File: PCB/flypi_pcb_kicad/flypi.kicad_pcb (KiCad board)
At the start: 2 copper layers, 76 x 93 mm, 44 parts, among them CON1 BARREL_JACK, J12 USB_A, P1 PeltS1S2, P10 RGB RG-B, P3 Fan+-, P4 Therm +s-, P5 HP1+-, P6 HP2+-, P7 servo +s-, P8 Ring +-s, P9 matrix +-scsd, Q1 1A_NPN_ECB, Q2 1A-NPN-ECB, Q3 1A_NPN_ECB, Q4 1A_NPN_ECB, U1 LM2596, U2 LM2596, U3 LM2596, U4 L298N, U5 arduino_mini

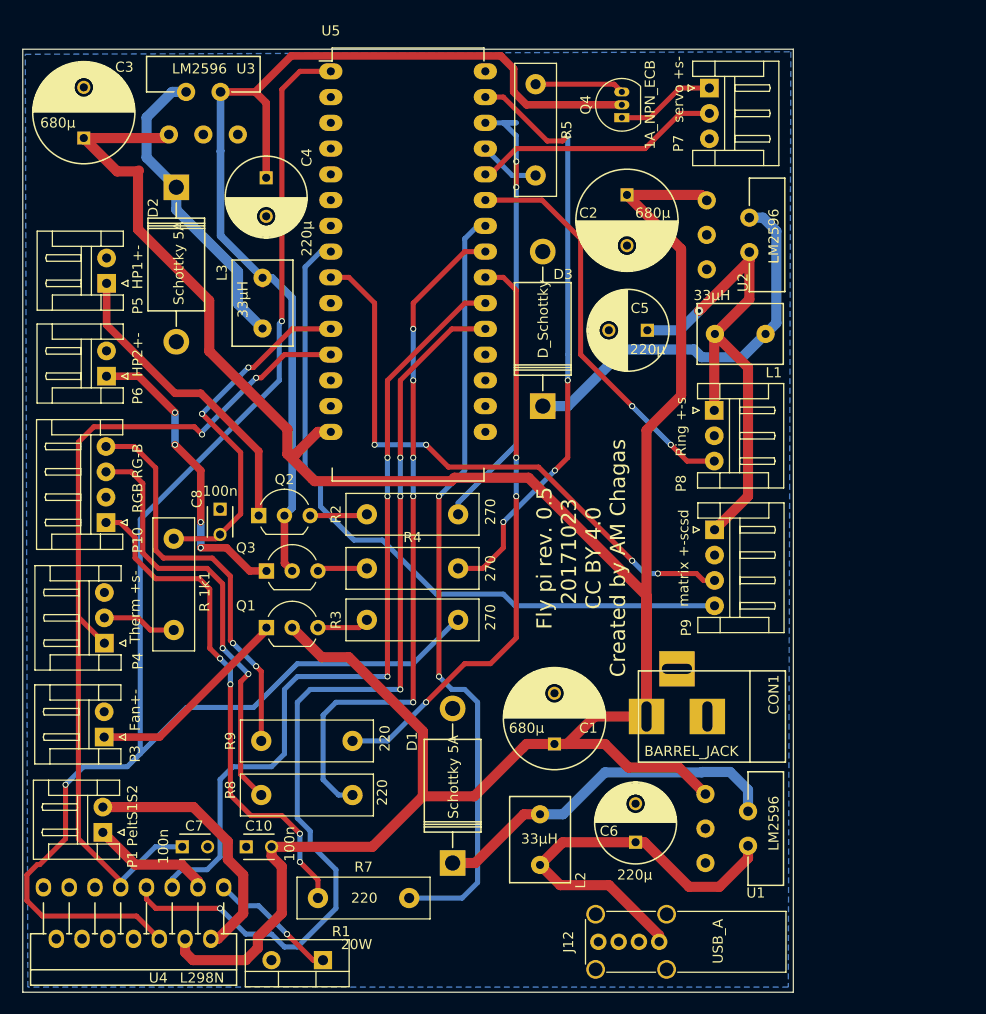
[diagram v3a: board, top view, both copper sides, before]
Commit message: update to pcb labels (corrected inverted values)
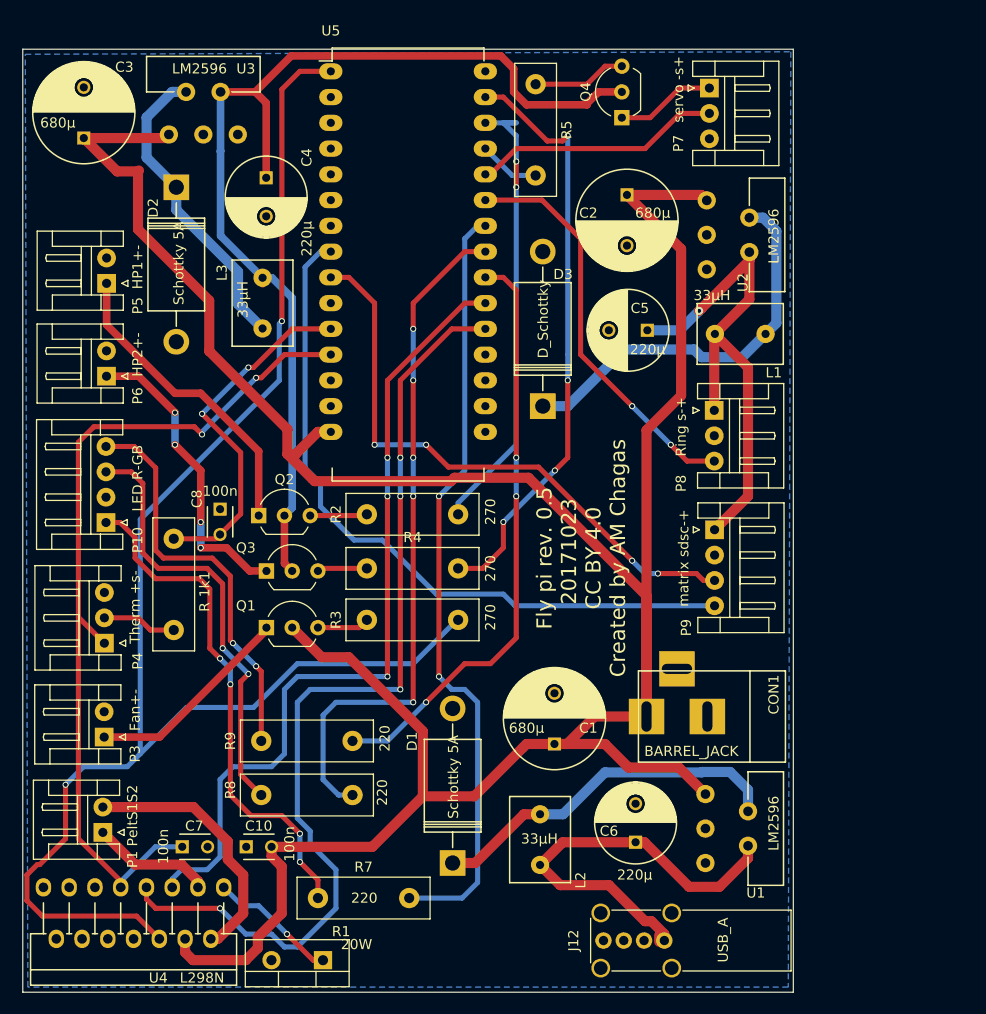
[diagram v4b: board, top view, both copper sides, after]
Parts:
- P10: value RGB RG-B -> LED R-GB
- P7: value servo +s- -> servo -s+
- P8: value Ring +-s -> Ring s-+
- P9: value matrix +-scsd -> matrix sdsc-+
- Q4: footprint TO_SOT_Packages_THT:TO-92_Inline_Narrow_Oval -> TO_SOT_Packages_THT:TO-92_Inline_Wide
- moved J12 0.52 mm to (168.3, 128.9)
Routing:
- net Net-(C6-Pad1): track 40.9 -> 42.0 mm
- net Net-(C4-Pad1): track 105.3 -> 105.9 mm
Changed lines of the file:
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@@
     (thickness 1.6)
     (drawings 12)
-    (tracks 445)
+    (tracks 452)
     (zones 0)
     (modules 44)
@@
   )
   (module Connectors:USB_A_Vertical (layer F.Cu)
-    (at 167.77 129.03 270)
+    (at 168.275 128.905 270)
     (descr "USB A vertical female connector, right angle")
     (tags "USB_A_Vertical female connector angled 73725-0110BLF")
@@
       (effects (font (size 1 1) (thickness 0.15)))
     )
-    (fp_text value "servo +s-" (at 0.128 3.048 270) (layer F.SilkS)
+    (fp_text value "servo -s+" (at 0.128 3.048 270) (layer F.SilkS)
       (effects (font (size 1 1) (thickness 0.15)))
     )
@@
       (effects (font (size 1 1) (thickness 0.15)))
     )
-    (fp_text value "Ring +-s" (at 1.612 3.274 270) (layer F.SilkS)
+    (fp_text value "Ring s-+" (at 1.612 3.274 270) (layer F.SilkS)
       (effects (font (size 1 1) (thickness 0.15)))
     )
@@
       (effects (font (size 1 1) (thickness 0.15)))
     )
-    (fp_text value "matrix +-scsd" (at 2.796 3.05 270) (layer F.SilkS)
+    (fp_text value "matrix sdsc-+" (at 2.796 3.05 270) (layer F.SilkS)
       (effects (font (size 1 1) (thickness 0.15)))
     )
@@
       (effects (font (size 1 1) (thickness 0.15)))
     )
-    (fp_text value "RGB RG-B" (at 4.368 3.122 90) (layer F.SilkS)
+    (fp_text value "LED R-GB" (at 4.368 3.122 90) (layer F.SilkS)
       (effects (font (size 1 1) (thickness 0.15)))
     )
@@
     )
   )
-  (module TO_SOT_Packages_THT:TO-92_Inline_Narrow_Oval (layer F.Cu)
-    (at 164.084 47.752 90)
-    (descr "TO-92 leads in-line, narrow, oval pads, drill 0.6mm (see NXP sot054_po.pdf)")
-    (tags "to-92 sc-43 sc-43a sot54 PA33 transistor")
-    (fp_text reference Q4 (at 1.27 -3.56 90) (layer F.SilkS)
-      (effects (font (size 1 1) (thickness 0.15)))
-    )
-    (fp_text value 1A_NPN_ECB (at 1.27 2.79 90) (layer F.SilkS)
-      (effects (font (size 1 1) (thickness 0.15)))
-    )
-    (fp_text user %R (at 1.27 -3.56 90) (layer F.Fab)
-      (effects (font (size 1 1) (thickness 0.15)))
-    )
-    (fp_line (start -0.53 1.85) (end 3.07 1.85) (layer F.SilkS) (width 0.12))
-    (fp_line (start -0.5 1.75) (end 3 1.75) (layer F.Fab) (width 0.1))
-    (fp_line (start -1.46 -2.73) (end 4 -2.73) (layer F.CrtYd) (width 0.05))
-    (fp_line (start -1.46 -2.73) (end -1.46 2.01) (layer F.CrtYd) (width 0.05))
-    (fp_line (start 4 2.01) (end 4 -2.73) (layer F.CrtYd) (width 0.05))
-    (fp_line (start 4 2.01) (end -1.46 2.01) (layer F.CrtYd) (width 0.05))
-    (fp_arc (start 1.27 0) (end 1.27 -2.48) (angle 135) (layer F.Fab) (width 0.1))
-    (fp_arc (start 1.27 0) (end 1.27 -2.6) (angle -135) (layer F.SilkS) (width 0.12))
-    (fp_arc (start 1.27 0) (end 1.27 -2.48) (angle -135) (layer F.Fab) (width 0.1))
-    (fp_arc (start 1.27 0) (end 1.27 -2.6) (angle 135) (layer F.SilkS) (width 0.12))
-    (pad 2 thru_hole oval (at 1.27 0 270) (size 0.9 1.5) (drill 0.6) (layers *.Cu *.Mask)
-      (net 4 "Net-(C4-Pad1)"))
-    (pad 3 thru_hole oval (at 2.54 0 270) (size 0.9 1.5) (drill 0.6) (layers *.Cu *.Mask)
-      (net 27 "Net-(Q4-Pad3)"))
-    (pad 1 thru_hole rect (at 0 0 270) (size 0.9 1.5) (drill 0.6) (layers *.Cu *.Mask)
-      (net 17 "Net-(P7-Pad1)"))
-    (model ${KISYS3DMOD}/TO_SOT_Packages_THT.3dshapes/TO-92_Inline_Narrow_Oval.wrl
-      (at (xyz 0.05 0 0))
-      (scale (xyz 1 1 1))
-      (rotate (xyz 0 0 -90))
-    )
-  )
   (module TO_SOT_Packages_THT:TO-220-2_Vertical (layer F.Cu)
     (at 134.61 130.84 180)
@@
     (pad 1 thru_hole rect (at 0 0 90) (size 1.52 1.52) (drill 0.8) (layers *.Cu *.Mask)
       (net 13 "Net-(P3-Pad1)"))
+    (model ${KISYS3DMOD}/TO_SOT_Packages_THT.3dshapes/TO-92_Inline_Wide.wrl
+      (at (xyz 0.1 0 0))
+      (scale (xyz 1 1 1))
+      (rotate (xyz 0 0 -90))
+    )
+  )
+  (module TO_SOT_Packages_THT:TO-92_Inline_Wide (layer F.Cu)
+    (at 164.084 47.752 90)
+    (descr "TO-92 leads in-line, wide, drill 0.8mm (see NXP sot054_po.pdf)")
+    (tags "to-92 sc-43 sc-43a sot54 PA33 transistor")
+    (fp_text reference Q4 (at 2.54 -3.56 270) (layer F.SilkS)
+      (effects (font (size 1 1) (thickness 0.15)))
+    )
+    (fp_text value 1A_NPN_ECB (at 2.54 2.79 90) (layer F.Fab)
+      (effects (font (size 1 1) (thickness 0.15)))
+    )
+    (fp_text user %R (at 2.54 -3.56 270) (layer F.Fab)
+      (effects (font (size 1 1) (thickness 0.15)))
+    )
+    (fp_line (start 0.74 1.85) (end 4.34 1.85) (layer F.SilkS) (width 0.12))
+    (fp_line (start 0.8 1.75) (end 4.3 1.75) (layer F.Fab) (width 0.1))
+    (fp_line (start -1.01 -2.73) (end 6.09 -2.73) (layer F.CrtYd) (width 0.05))
+    (fp_line (start -1.01 -2.73) (end -1.01 2.01) (layer F.CrtYd) (width 0.05))
+    (fp_line (start 6.09 2.01) (end 6.09 -2.73) (layer F.CrtYd) (width 0.05))
+    (fp_line (start 6.09 2.01) (end -1.01 2.01) (layer F.CrtYd) (width 0.05))
+    (fp_arc (start 2.54 0) (end 0.74 1.85) (angle 20) (layer F.SilkS) (width 0.12))
+    (fp_arc (start 2.54 0) (end 2.54 -2.6) (angle -65) (layer F.SilkS) (width 0.12))
+    (fp_arc (start 2.54 0) (end 2.54 -2.6) (angle 65) (layer F.SilkS) (width 0.12))
+    (fp_arc (start 2.54 0) (end 2.54 -2.48) (angle 135) (layer F.Fab) (width 0.1))
+    (fp_arc (start 2.54 0) (end 2.54 -2.48) (angle -135) (layer F.Fab) (width 0.1))
+    (fp_arc (start 2.54 0) (end 4.34 1.85) (angle -20) (layer F.SilkS) (width 0.12))
+    (pad 2 thru_hole circle (at 2.54 0 180) (size 1.52 1.52) (drill 0.8) (layers *.Cu *.Mask)
+      (net 4 "Net-(C4-Pad1)"))
+    (pad 3 thru_hole circle (at 5.08 0 180) (size 1.52 1.52) (drill 0.8) (layers *.Cu *.Mask)
+      (net 27 "Net-(Q4-Pad3)"))
+    (pad 1 thru_hole rect (at 0 0 180) (size 1.52 1.52) (drill 0.8) (layers *.Cu *.Mask)
+      (net 17 "Net-(P7-Pad1)"))
     (model ${KISYS3DMOD}/TO_SOT_Packages_THT.3dshapes/TO-92_Inline_Wide.wrl
       (at (xyz 0.1 0 0))
@@
   (segment (start 158.15 109.52) (end 157.44 109.52) (width 1) (layer F.Cu) (net 3))
   (segment (start 161.4 106.81) (end 158.69 109.52) (width 1) (layer F.Cu) (net 3))
+  (segment (start 160.655 46.482) (end 160.655 46.355) (width 0.75) (layer F.Cu) (net 4))
+  (segment (start 161.798 45.212) (end 164.084 45.212) (width 0.75) (layer F.Cu) (net 4))
+  (segment (start 160.655 46.355) (end 161.798 45.212) (width 0.75) (layer F.Cu) (net 4))
   (segment (start 130.81 86.995) (end 130.81 91.694) (width 0.75) (layer F.Cu) (net 4))
   (segment (start 130.81 91.694) (end 131.572 92.456) (width 0.75) (layer F.Cu) (net 4))
@@
   (segment (start 131.572 65.532) (end 131.572 86.233) (width 0.75) (layer B.Cu) (net 4))
   (segment (start 129.58064 63.54064) (end 131.572 65.532) (width 0.75) (layer B.Cu) (net 4))
-  (segment (start 164.084 46.482) (end 154.686 46.482) (width 0.75) (layer F.Cu) (net 4))
+  (segment (start 160.655 46.482) (end 154.686 46.482) (width 0.75) (layer F.Cu) (net 4))
   (segment (start 131.484 41.656) (end 127.93 45.21) (width 0.75) (layer F.Cu) (net 4))
   (segment (start 152.146 41.656) (end 131.484 41.656) (width 0.75) (layer F.Cu) (net 4))
@@
   (segment (start 176.66 61.01) (end 176.66 65.68064) (width 1) (layer F.Cu) (net 5))
   (segment (start 176.66 65.68064) (end 173.26064 69.08) (width 1) (layer F.Cu) (net 5))
+  (segment (start 166.37 127) (end 167.005 127) (width 1) (layer F.Cu) (net 6))
+  (segment (start 167.005 127) (end 168.275 128.27) (width 1) (layer F.Cu) (net 6))
+  (segment (start 168.275 128.27) (end 168.275 128.905) (width 1) (layer F.Cu) (net 6))
   (segment (start 167.77 129.03) (end 167.77 128.4) (width 1) (layer F.Cu) (net 6))
-  (segment (start 167.77 128.4) (end 162.814 123.444) (width 1) (layer F.Cu) (net 6))
+  (segment (start 166.37 127) (end 162.814 123.444) (width 1) (layer F.Cu) (net 6))
   (segment (start 162.814 123.444) (end 158.01464 123.444) (width 1) (layer F.Cu) (net 6))
   (segment (start 158.01464 123.444) (end 156.02 121.44936) (width 1) (layer F.Cu) (net 6))
@@
   (segment (start 134.366 92.202) (end 134.112 92.456) (width 0.5) (layer F.Cu) (net 26))
   (segment (start 138.684 91.948) (end 138.938 92.202) (width 0.5) (layer F.Cu) (net 26))
-  (segment (start 155.58 44.45) (end 163.322 44.45) (width 0.5) (layer F.Cu) (net 27))
-  (segment (start 163.322 44.45) (end 164.084 45.212) (width 0.5) (layer F.Cu) (net 27))
+  (segment (start 155.58 44.45) (end 160.655 44.45) (width 0.5) (layer F.Cu) (net 27))
+  (segment (start 162.433 42.672) (end 164.084 42.672) (width 0.5) (layer F.Cu) (net 27))
+  (segment (start 160.655 44.45) (end 162.433 42.672) (width 0.5) (layer F.Cu) (net 27))
   (segment (start 150.622 48.26) (end 153.67 48.26) (width 0.5) (layer B.Cu) (net 28))
   (segment (start 147.938 85.742) (end 147.938 86.868) (width 0.5) (layer B.Cu) (net 28))

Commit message: updated the PCB. Removed one of the voltage regulators (as everything seem to work fine with just 2. Changed the plugs so that the cables cab be bought crimmped.)
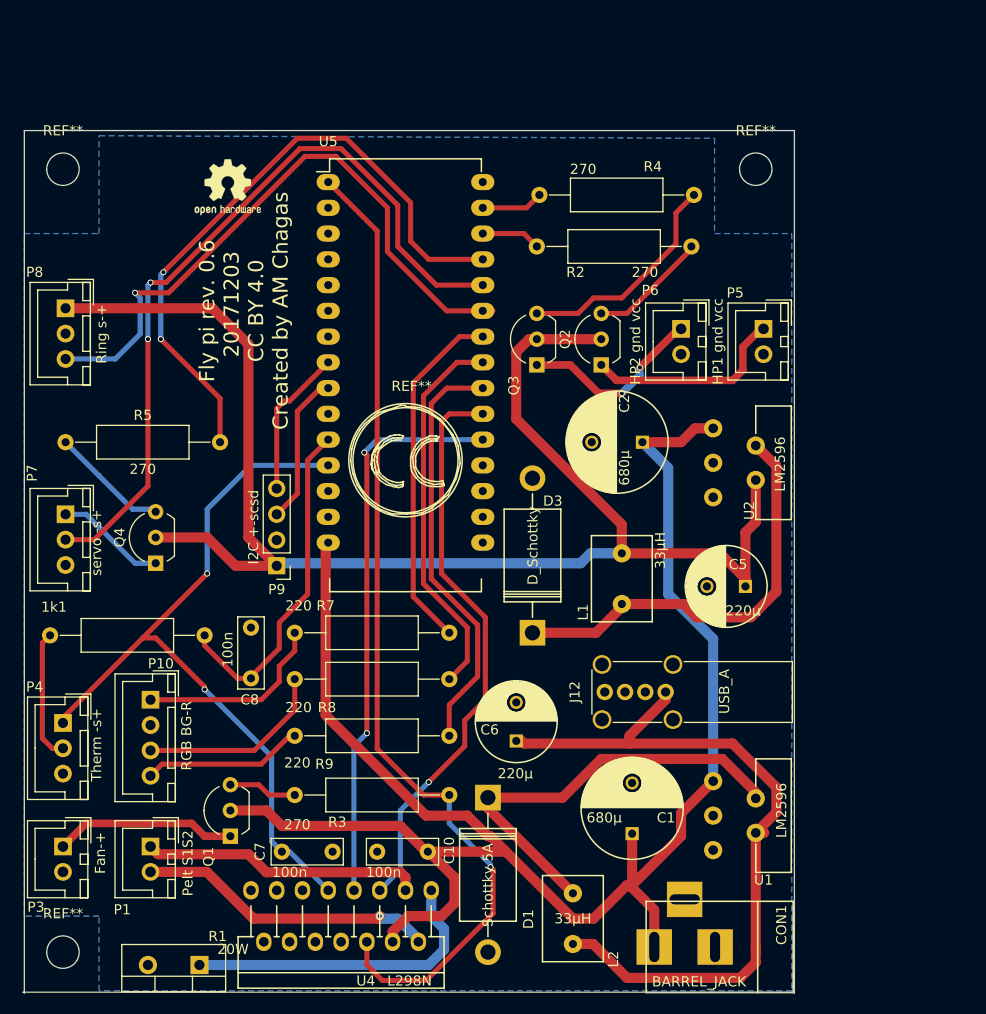
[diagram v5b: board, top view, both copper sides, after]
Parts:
- removed C3: 680µ, Capacitors_ThroughHole:C_Radial_D10_L21_P5
- removed C4: 220µ, Capacitors_ThroughHole:C_Radial_D8_L13_P3.8
- removed D2: Schottky 5A, Diodes_ThroughHole:Diode_DO-201AD_Horizontal_RM15
- removed L3: 33µH, Inductors_NEOSID:Neosid_Inductor_MA-Bs75
- removed U3: LM2596, footprints:LM2596
- added REF**: MountingHole_3.2mm_M3_DIN965, Mounting_Holes:MountingHole_3.2mm_M3_DIN965, F.Cu at (109.0, 130.0)
- added REF**: MountingHole_3.2mm_M3_DIN965, Mounting_Holes:MountingHole_3.2mm_M3_DIN965, F.Cu at (109.0, 52.8)
- added REF**: MountingHole_3.2mm_M3_DIN965, Mounting_Holes:MountingHole_3.2mm_M3_DIN965, F.Cu at (177.3, 52.8)
- added REF**: Symbol_CreativeCommons_SilkScreenTop_Type2_Big, Symbols:Symbol_CreativeCommons_SilkScreenTop_Type2_Big, F.Cu at (142.7, 81.5)
- added REF***: OSHW-Logo2_7.3x6mm_SilkScreen, Symbols:OSHW-Logo2_7.3x6mm_SilkScreen, F.Cu at (125.2, 54.6)
- 1k1, R2, R3, R4, R5, R7, R8, R9: footprint Resistors_THT:R_Box_L13.0mm_W4.0mm_P9.00mm -> Resistors_THT:R_Axial_DIN0309_L9.0mm_D3.2mm_P15.24mm_Horizontal
- C10, C7, C8: footprint Capacitors_ThroughHole:C_Disc_D3_P2.5 -> Capacitors_THT:C_Rect_L7.0mm_W2.5mm_P5.00mm
- P1: value PeltS1S2 -> Pelt S1S2; footprint Connectors_JST:JST_EH_S02B-EH_02x2.50mm_Angled -> Connectors_JST:JST_XH_B02B-XH-A_02x2.50mm_Straight
- P10: value LED R-GB -> RGB BG-R; footprint Connectors_JST:JST_EH_S04B-EH_04x2.50mm_Angled -> Connectors_JST:JST_XH_B04B-XH-A_04x2.50mm_Straight
- P3: value Fan+- -> Fan-+; footprint Connectors_JST:JST_EH_S02B-EH_02x2.50mm_Angled -> Connectors_JST:JST_XH_B02B-XH-A_02x2.50mm_Straight
- P4: value Therm +s- -> Therm -s+; footprint Connectors_JST:JST_EH_S03B-EH_03x2.50mm_Angled -> Connectors_JST:JST_XH_B03B-XH-A_03x2.50mm_Straight
- P5: value HP1+- -> HP1 gnd vcc; footprint Connectors_JST:JST_EH_S02B-EH_02x2.50mm_Angled -> Connectors_JST:JST_XH_B02B-XH-A_02x2.50mm_Straight
- P6: value HP2+- -> HP2 gnd vcc; footprint Connectors_JST:JST_EH_S02B-EH_02x2.50mm_Angled -> Connectors_JST:JST_XH_B02B-XH-A_02x2.50mm_Straight
- P7, P8: footprint Connectors_JST:JST_EH_S03B-EH_03x2.50mm_Angled -> Connectors_JST:JST_XH_B03B-XH-A_03x2.50mm_Straight
- P9: value matrix sdsc-+ -> I2C +-scsd; footprint Connectors_JST:JST_EH_S04B-EH_04x2.50mm_Angled -> Socket_Strips:Socket_Strip_Straight_1x04_Pitch2.54mm
- moved P7 76.2 mm to (109.2, 86.9)
- moved P5 64.9 mm to (178.1, 68.6), turned to 270 degrees
- moved P8 64.8 mm to (109.2, 66.5)
- moved Q4 63.6 mm to (118.1, 91.7)
- moved R5 58.3 mm to (109.2, 79.8), turned to 0 degrees
- moved P6 56.9 mm to (169.9, 68.6), turned to 270 degrees
- moved R4 49.0 mm to (171.2, 55.4), turned to 180 degrees
- moved P9 43.3 mm to (130.0, 91.9), turned to 180 degrees
- moved R2 41.5 mm to (170.9, 60.5), turned to 180 degrees
- moved Q2 36.9 mm to (162.1, 72.1), turned to 90 degrees
- moved Q3 33.5 mm to (155.7, 72.1), turned to 90 degrees
- moved C5 27.0 mm to (176.3, 94.0)
- moved L1 26.8 mm to (164.1, 93.2), turned to 90 degrees
- moved R7 26.3 mm to (131.8, 98.6)
- moved J12 24.5 mm to (168.4, 104.4)
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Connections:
- J12 pad 2: Net-(J12-Pad2) -> (no net)
- J12 pad 3: Net-(J12-Pad3) -> (no net)
- Q2 pad 2: Net-(C4-Pad1) -> Net-(C5-Pad1)
- Q3 pad 2: Net-(C4-Pad1) -> Net-(C5-Pad1)
- Q4 pad 2: Net-(C4-Pad1) -> Net-(C5-Pad1)
- U4 pad 10: Net-(U4-Pad10) -> (no net)
- U4 pad 11: Net-(U4-Pad11) -> (no net)
- U4 pad 12: Net-(U4-Pad12) -> (no net)
- U4 pad 13: Net-(U4-Pad13) -> (no net)
- U4 pad 14: Net-(U4-Pad14) -> (no net)
- U4 pad 15: Net-(U4-Pad15) -> (no net)
- U5 pad 10: Net-(U5-Pad10) -> (no net)
- U5 pad 13: Net-(U5-Pad13) -> (no net)
- U5 pad 16: Net-(U5-Pad16) -> (no net)
- U5 pad 17: Net-(U5-Pad17) -> (no net)
- U5 pad 18: Net-(U5-Pad18) -> (no net)
- U5 pad 2: Net-(U5-Pad2) -> (no net)
- U5 pad 3: Net-(U5-Pad3) -> (no net)
- U5 pad 30: Net-(U5-Pad30) -> (no net)
- U5 pad 4: Net-(U5-Pad4) -> (no net)
- U5 pad 5: Net-(U5-Pad5) -> (no net)
- U5 pad 6: Net-(U5-Pad6) -> (no net)
- U5 pad 7: Net-(U5-Pad7) -> (no net)
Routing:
- net Net-(C4-Pad1): track 105.9 -> 0.00 mm
- net Net-(C1-Pad1): track 273.8 -> 170.1 mm
- net Net-(C5-Pad1): track 52.8 -> 148.1 mm, vias 1 -> 0
- net Net-(R5-Pad2): track 6.07 -> 63.4 mm, vias 0 -> 2
- net Net-(P9-Pad4): track 70.3 -> 14.8 mm
- net Net-(R4-Pad2): track 58.7 -> 6.11 mm, vias 4 -> 0
- net Net-(R3-Pad2): track 150.1 -> 98.5 mm, vias 2 -> 1
- net Net-(P7-Pad2): track 25.3 -> 76.7 mm, vias 0 -> 2
- net Net-(P9-Pad3): track 58.4 -> 15.0 mm, vias 4 -> 0
- net Net-(U4-Pad7): track 98.2 -> 56.0 mm, vias 4 -> 2
- net Net-(R7-Pad2): track 76.8 -> 34.9 mm, vias 2 -> 0
- net Net-(R2-Pad2): track 46.2 -> 5.86 mm, vias 2 -> 0
- net Net-(P10-Pad1): track 50.8 -> 18.9 mm, vias 4 -> 0
- net Net-(C6-Pad1): track 42.0 -> 73.1 mm
- net Net-(R8-Pad2): track 68.5 -> 37.7 mm, vias 5 -> 0
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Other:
- board size 76 x 93 mm -> 76.1 x 85.1 mm
- board text added: "Fly pi rev. 0.6 20171203 CC BY 4.0 Created by AM Chagas"
- board text added: "www.prometheus-science.com https://github.com/prometheus-science/Flypi"
- board text removed: "Fly pi rev. 0.5 20171023 CC BY 4.0 Created by AM Chagas"
